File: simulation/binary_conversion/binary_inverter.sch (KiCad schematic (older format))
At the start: 2 parts, among them M1 BSS84, M2 2N7002

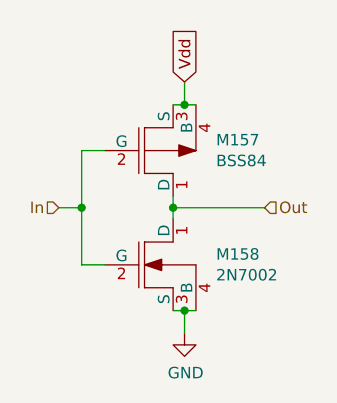
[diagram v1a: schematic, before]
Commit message: update readme.md to include current project status
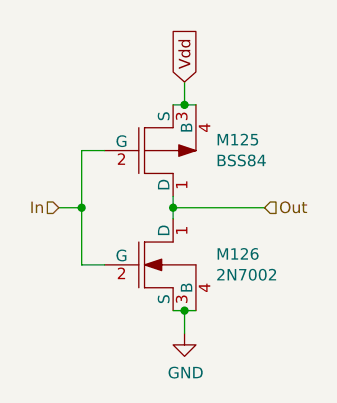
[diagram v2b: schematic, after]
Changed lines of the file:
@@
 AR Path="/5FEFDA4D/6206C5AA/5FECF196" Ref="M148"  Part="1"
 AR Path="/5FEFDF88/6206C5AA/5FECF196" Ref="M146"  Part="1"
-F 0 "M158" H 5838 3896 50  0000 L CNN
+F 0 "M126" H 5838 3896 50  0000 L CNN
 F 1 "2N7002" H 5838 3805 50  0000 L CNN
 F 2 "" H 5525 3850 50  0001 C CNN
@@
 AR Path="/5FEFDA4D/6206C5AA/5FECF1A0" Ref="M147"  Part="1"
 AR Path="/5FEFDF88/6206C5AA/5FECF1A0" Ref="M145"  Part="1"
-F 0 "M157" H 5838 3396 50  0000 L CNN
+F 0 "M125" H 5838 3396 50  0000 L CNN
 F 1 "BSS84" H 5838 3305 50  0000 L CNN
 F 2 "" H 5550 3350 50  0001 C CNN
@@
 AR Path="/5FEFDA4D/6206C5AA/5FED643A" Ref="#PWR099"  Part="1"
 AR Path="/5FEFDF88/6206C5AA/5FED643A" Ref="#PWR098"  Part="1"
-F 0 "#PWR0104" H 5700 3900 50  0001 C CNN
+F 0 "#PWR088" H 5700 3900 50  0001 C CNN
 F 1 "GND" H 5705 3977 50  0000 C CNN
 F 2 "" H 5700 4150 50  0001 C CNN
